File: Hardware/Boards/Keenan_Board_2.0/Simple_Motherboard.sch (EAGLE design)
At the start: 100 parts, among them U1 WIZ811MJ, U1_MUX 74HC4052D,653, U2_MUX 74HC4052D,653, U3_MUX 74HC4052D,653, U4_MUX 74HC4052D,653, U5_MUX 74HC4052D,653, U7_MUX 74HC4052D,653

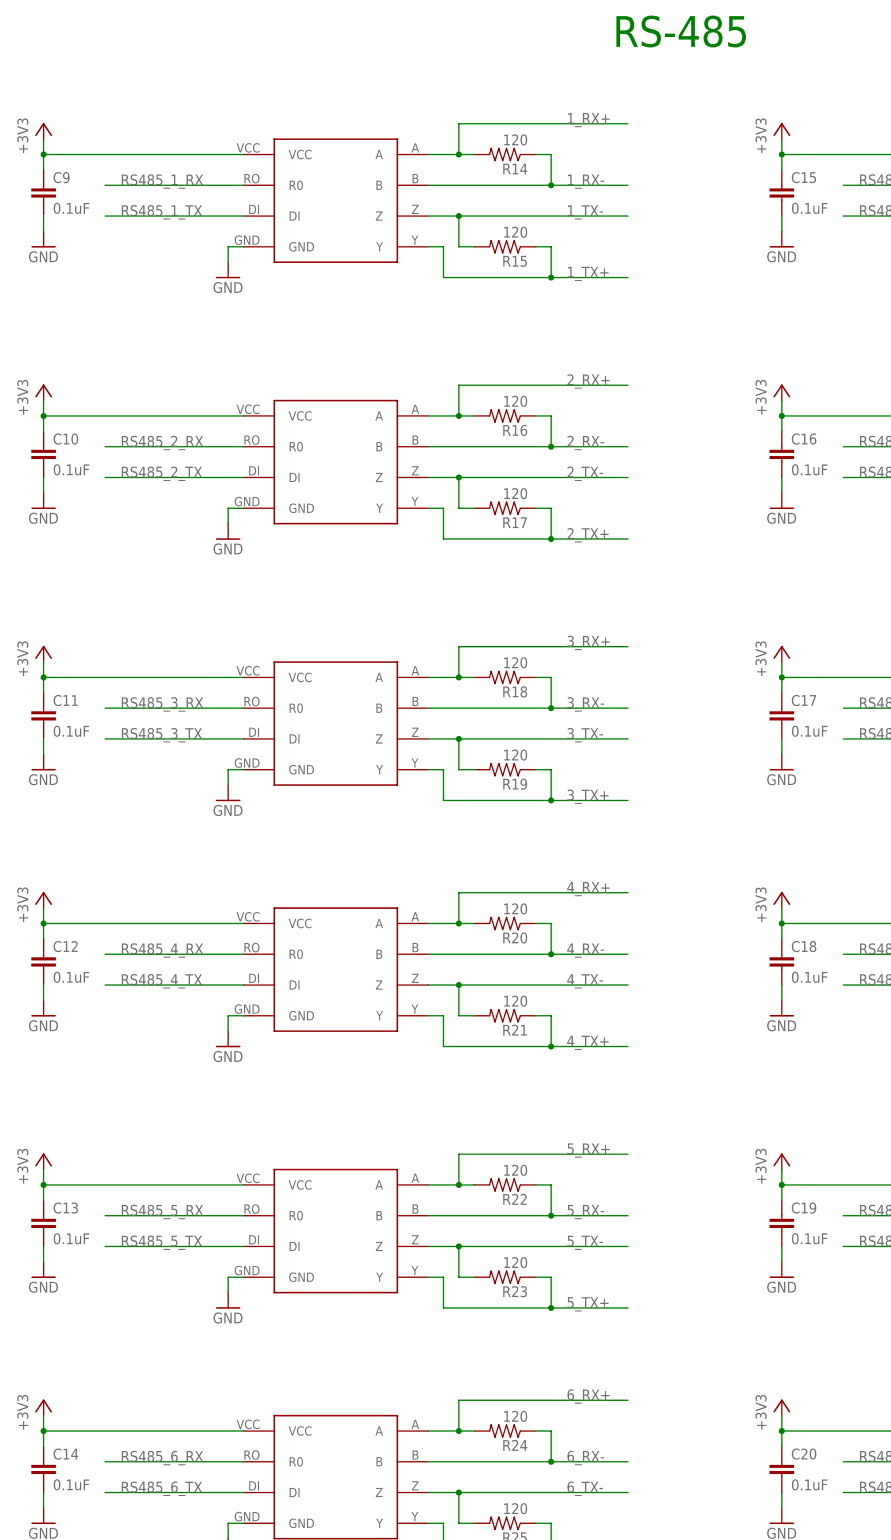
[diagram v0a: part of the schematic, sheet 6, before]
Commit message: Changed muxes back to 5V power.
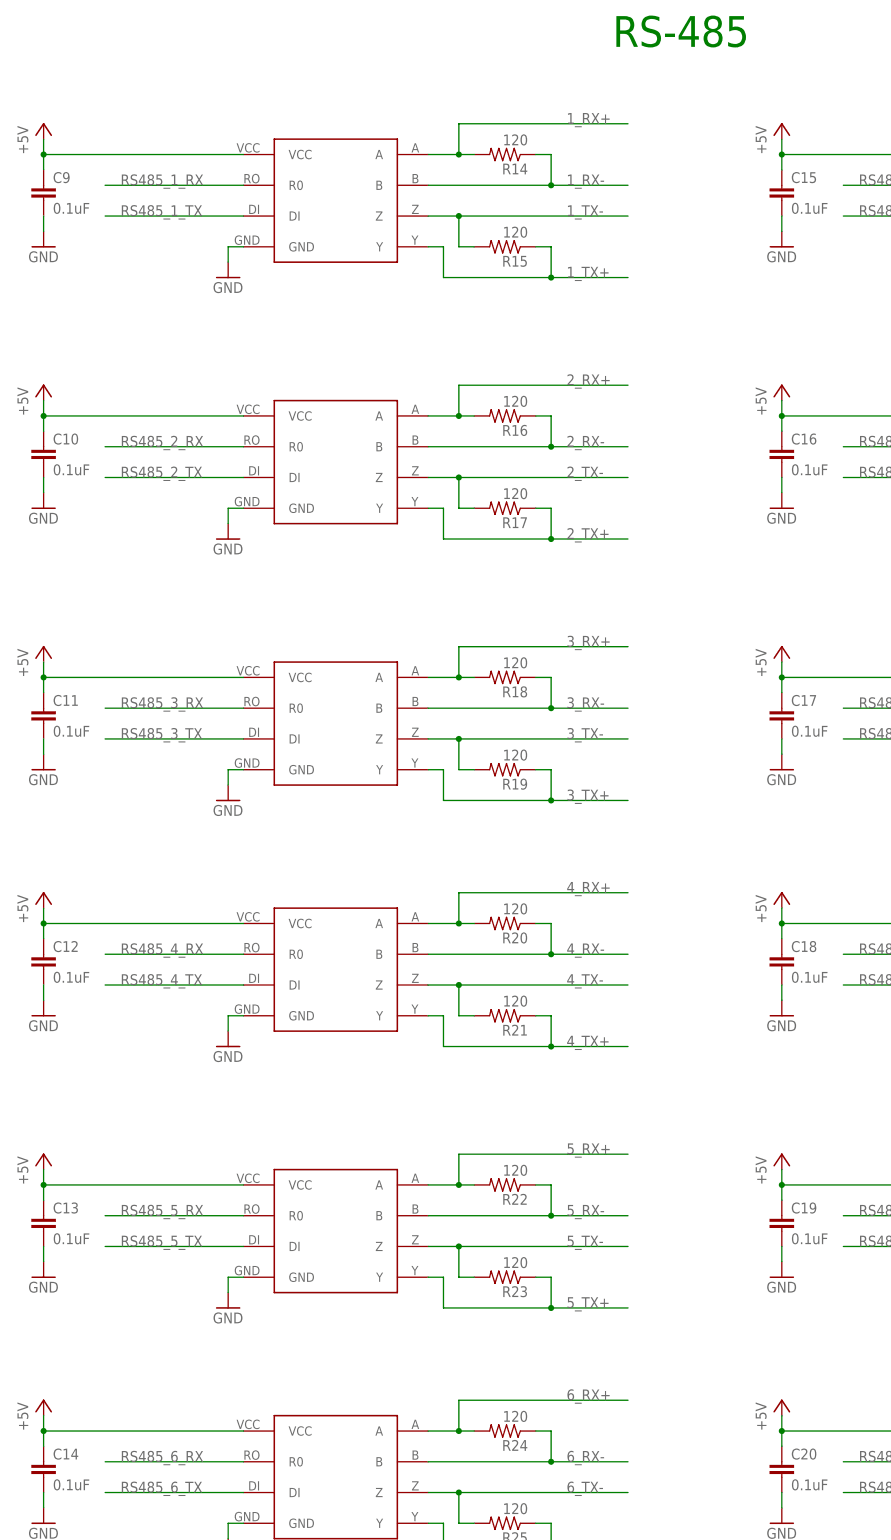
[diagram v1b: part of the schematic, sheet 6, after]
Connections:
- net +3V3: no longer C10.1, C11.1, C12.1, C13.1, C14.1, C15.1, C16.1, C17.1, C18.1, C19.1, C20.1, C3.1, C4.1, C5.1, C6.1, C7.1, C8.1, C9.1, RS-485-1.VCC, RS-485-2.VCC, RS-485-3.VCC, RS-485-4.VCC, RS-485-5.VCC, RS-485-6.VCC, RS_TRANS_1.VCC, RS_TRANS_10.VCC, RS_TRANS_11.VCC, RS_TRANS_12.VCC, RS_TRANS_2.VCC, RS_TRANS_3.VCC, RS_TRANS_4.VCC, RS_TRANS_5.VCC, RS_TRANS_6.VCC, RS_TRANS_7.VCC, RS_TRANS_8.VCC, RS_TRANS_9.VCC
- net +5V: now also C10.1, C11.1, C12.1, C13.1, C14.1, C15.1, C16.1, C17.1, C18.1, C19.1, C20.1, C3.1, C4.1, C5.1, C6.1, C7.1, C8.1, C9.1, RS-485-1.VCC, RS-485-2.VCC, RS-485-3.VCC, RS-485-4.VCC, RS-485-5.VCC, RS-485-6.VCC, RS_TRANS_1.VCC, RS_TRANS_10.VCC, RS_TRANS_11.VCC, RS_TRANS_12.VCC, RS_TRANS_2.VCC, RS_TRANS_3.VCC, RS_TRANS_4.VCC, RS_TRANS_5.VCC, RS_TRANS_6.VCC, RS_TRANS_7.VCC, RS_TRANS_8.VCC, RS_TRANS_9.VCC

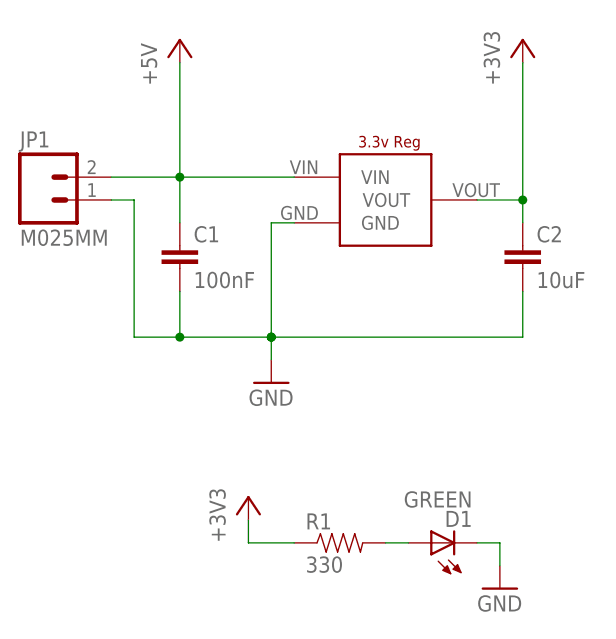
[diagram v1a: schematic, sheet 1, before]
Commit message: Routing power work
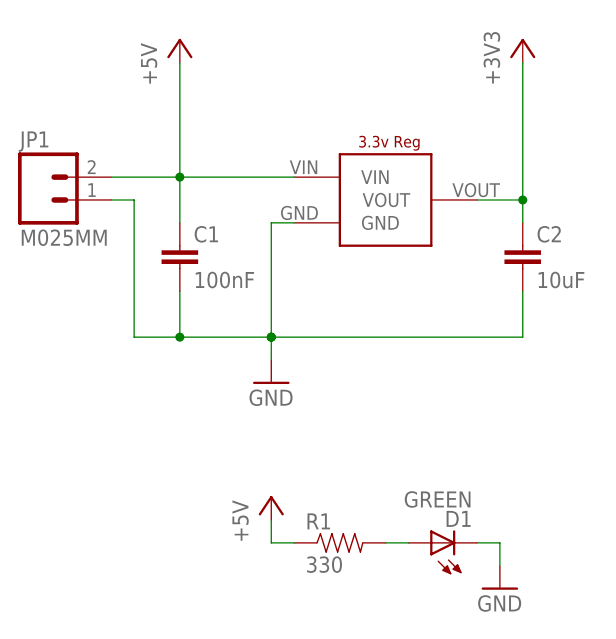
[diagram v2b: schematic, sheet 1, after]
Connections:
- net +3V3: no longer R1.1
- net +5V: now also R1.1, U7_MUX.VCC
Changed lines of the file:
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@@
 <part name="D1" library="SparkFun-LED" deviceset="LED-GREEN" device="LARGE" value="GREEN"/>
 <part name="GND94" library="supply1" deviceset="GND" device=""/>
-<part name="+3V53" library="supply1" deviceset="+3V3" device=""/>
 <part name="R1" library="SparkFun-Passives" deviceset="RESISTOR" device="1206" value="330"/>
 <part name="P+5" library="supply1" deviceset="+5V" device=""/>
@@
 <part name="P+25" library="supply1" deviceset="+5V" device=""/>
 <part name="P+26" library="supply1" deviceset="+5V" device=""/>
+<part name="P+27" library="supply1" deviceset="+5V" device=""/>
 </parts>
 <sheets>
@@
 <instance part="D1" gate="G$1" x="7.62" y="-17.78" rot="R90"/>
 <instance part="GND94" gate="1" x="15.24" y="-22.86"/>
-<instance part="+3V53" gate="G$1" x="-12.7" y="-12.7"/>
 <instance part="R1" gate="G$1" x="-2.54" y="-17.78"/>
 <instance part="P+5" gate="1" x="-20.32" y="38.1"/>
+<instance part="P+27" gate="1" x="-10.16" y="-12.7"/>
 </instances>
 <busses>
@@
 <nets>
 <net name="+3V3" class="0">
-<segment>
-<pinref part="+3V53" gate="G$1" pin="+3V3"/>
-<wire x1="-12.7" y1="-15.24" x2="-12.7" y2="-17.78" width="0.1524" layer="91"/>
-<pinref part="R1" gate="G$1" pin="1"/>
-<wire x1="-12.7" y1="-17.78" x2="-7.62" y2="-17.78" width="0.1524" layer="91"/>
-</segment>
 <segment>
 <pinref part="U$1" gate="G$1" pin="VOUT"/>
@@
 <pinref part="P+5" gate="1" pin="+5V"/>
 <wire x1="-20.32" y1="22.86" x2="-20.32" y2="35.56" width="0.1524" layer="91"/>
+</segment>
+<segment>
+<pinref part="P+27" gate="1" pin="+5V"/>
+<wire x1="-10.16" y1="-15.24" x2="-10.16" y2="-17.78" width="0.1524" layer="91"/>
+<pinref part="R1" gate="G$1" pin="1"/>
+<wire x1="-10.16" y1="-17.78" x2="-7.62" y2="-17.78" width="0.1524" layer="91"/>
 </segment>
 </net>
@@
 </segment>
 <segment>
+<pinref part="C26" gate="G$1" pin="1"/>
+<pinref part="P+7" gate="1" pin="+5V"/>
+<wire x1="66.04" y1="-17.78" x2="66.04" y2="-15.24" width="0.1524" layer="91"/>
+<pinref part="U7_MUX" gate="A" pin="VCC"/>
+<wire x1="66.04" y1="-15.24" x2="66.04" y2="-12.7" width="0.1524" layer="91"/>
 <wire x1="99.06" y1="-15.24" x2="66.04" y2="-15.24" width="0.1524" layer="91"/>
-<pinref part="C26" gate="G$1" pin="1"/>
-<wire x1="66.04" y1="-15.24" x2="66.04" y2="-17.78" width="0.1524" layer="91"/>
-<pinref part="P+7" gate="1" pin="+5V"/>
-<wire x1="66.04" y1="-15.24" x2="66.04" y2="-12.7" width="0.1524" layer="91"/>
 <junction x="66.04" y="-15.24"/>
 </segment>

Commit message: More routing
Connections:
- net +5V: now also U2_MUX.VCC, U3_MUX.VCC, U4_MUX.VCC, U5_MUX.VCC
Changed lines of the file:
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@@
 </segment>
 <segment>
+<pinref part="C22" gate="G$1" pin="1"/>
+<pinref part="P+2" gate="1" pin="+5V"/>
+<wire x1="-50.8" y1="40.64" x2="-50.8" y2="43.18" width="0.1524" layer="91"/>
+<pinref part="U2_MUX" gate="A" pin="VCC"/>
+<wire x1="-50.8" y1="43.18" x2="-50.8" y2="45.72" width="0.1524" layer="91"/>
 <wire x1="-17.78" y1="43.18" x2="-50.8" y2="43.18" width="0.1524" layer="91"/>
-<pinref part="C22" gate="G$1" pin="1"/>
-<wire x1="-50.8" y1="43.18" x2="-50.8" y2="40.64" width="0.1524" layer="91"/>
-<pinref part="P+2" gate="1" pin="+5V"/>
-<wire x1="-50.8" y1="43.18" x2="-50.8" y2="45.72" width="0.1524" layer="91"/>
 <junction x="-50.8" y="43.18"/>
 </segment>
 <segment>
+<pinref part="C23" gate="G$1" pin="1"/>
+<pinref part="P+3" gate="1" pin="+5V"/>
+<wire x1="66.04" y1="40.64" x2="66.04" y2="43.18" width="0.1524" layer="91"/>
+<pinref part="U3_MUX" gate="A" pin="VCC"/>
+<wire x1="66.04" y1="43.18" x2="66.04" y2="45.72" width="0.1524" layer="91"/>
 <wire x1="99.06" y1="43.18" x2="66.04" y2="43.18" width="0.1524" layer="91"/>
-<pinref part="C23" gate="G$1" pin="1"/>
-<wire x1="66.04" y1="43.18" x2="66.04" y2="40.64" width="0.1524" layer="91"/>
-<pinref part="P+3" gate="1" pin="+5V"/>
-<wire x1="66.04" y1="43.18" x2="66.04" y2="45.72" width="0.1524" layer="91"/>
 <junction x="66.04" y="43.18"/>
 </segment>
 <segment>
+<pinref part="C24" gate="G$1" pin="1"/>
+<pinref part="P+4" gate="1" pin="+5V"/>
+<wire x1="-165.1" y1="-17.78" x2="-165.1" y2="-15.24" width="0.1524" layer="91"/>
+<pinref part="U4_MUX" gate="A" pin="VCC"/>
+<wire x1="-165.1" y1="-15.24" x2="-165.1" y2="-12.7" width="0.1524" layer="91"/>
 <wire x1="-132.08" y1="-15.24" x2="-165.1" y2="-15.24" width="0.1524" layer="91"/>
-<pinref part="C24" gate="G$1" pin="1"/>
-<wire x1="-165.1" y1="-15.24" x2="-165.1" y2="-17.78" width="0.1524" layer="91"/>
-<pinref part="P+4" gate="1" pin="+5V"/>
-<wire x1="-165.1" y1="-15.24" x2="-165.1" y2="-12.7" width="0.1524" layer="91"/>
 <junction x="-165.1" y="-15.24"/>
 </segment>
 <segment>
+<pinref part="C25" gate="G$1" pin="1"/>
+<pinref part="P+6" gate="1" pin="+5V"/>
+<wire x1="-50.8" y1="-17.78" x2="-50.8" y2="-15.24" width="0.1524" layer="91"/>
+<pinref part="U5_MUX" gate="A" pin="VCC"/>
+<wire x1="-50.8" y1="-15.24" x2="-50.8" y2="-12.7" width="0.1524" layer="91"/>
 <wire x1="-17.78" y1="-15.24" x2="-50.8" y2="-15.24" width="0.1524" layer="91"/>
-<pinref part="C25" gate="G$1" pin="1"/>
-<wire x1="-50.8" y1="-15.24" x2="-50.8" y2="-17.78" width="0.1524" layer="91"/>
-<pinref part="P+6" gate="1" pin="+5V"/>
-<wire x1="-50.8" y1="-15.24" x2="-50.8" y2="-12.7" width="0.1524" layer="91"/>
 <junction x="-50.8" y="-15.24"/>
 </segment>

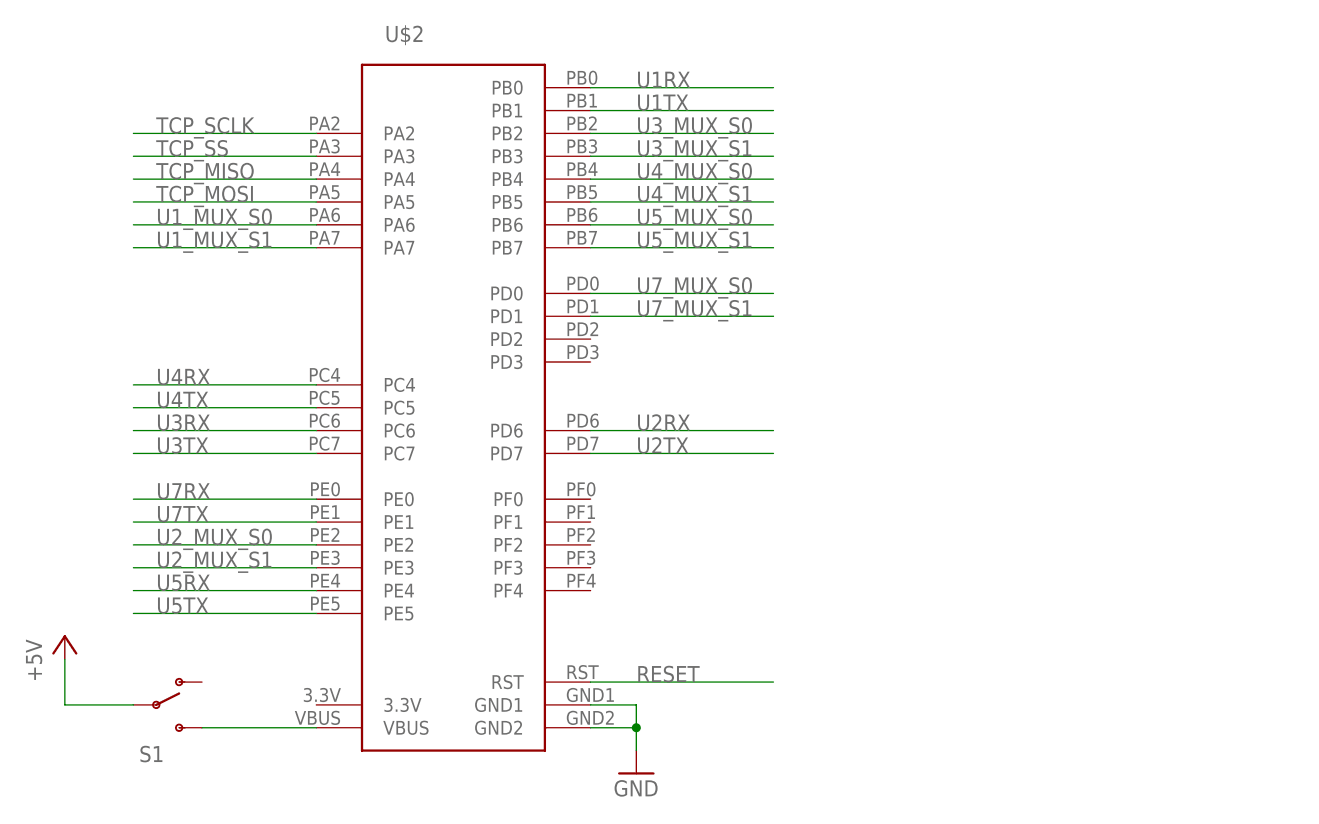
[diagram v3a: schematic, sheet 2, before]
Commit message: Added LCD Headers
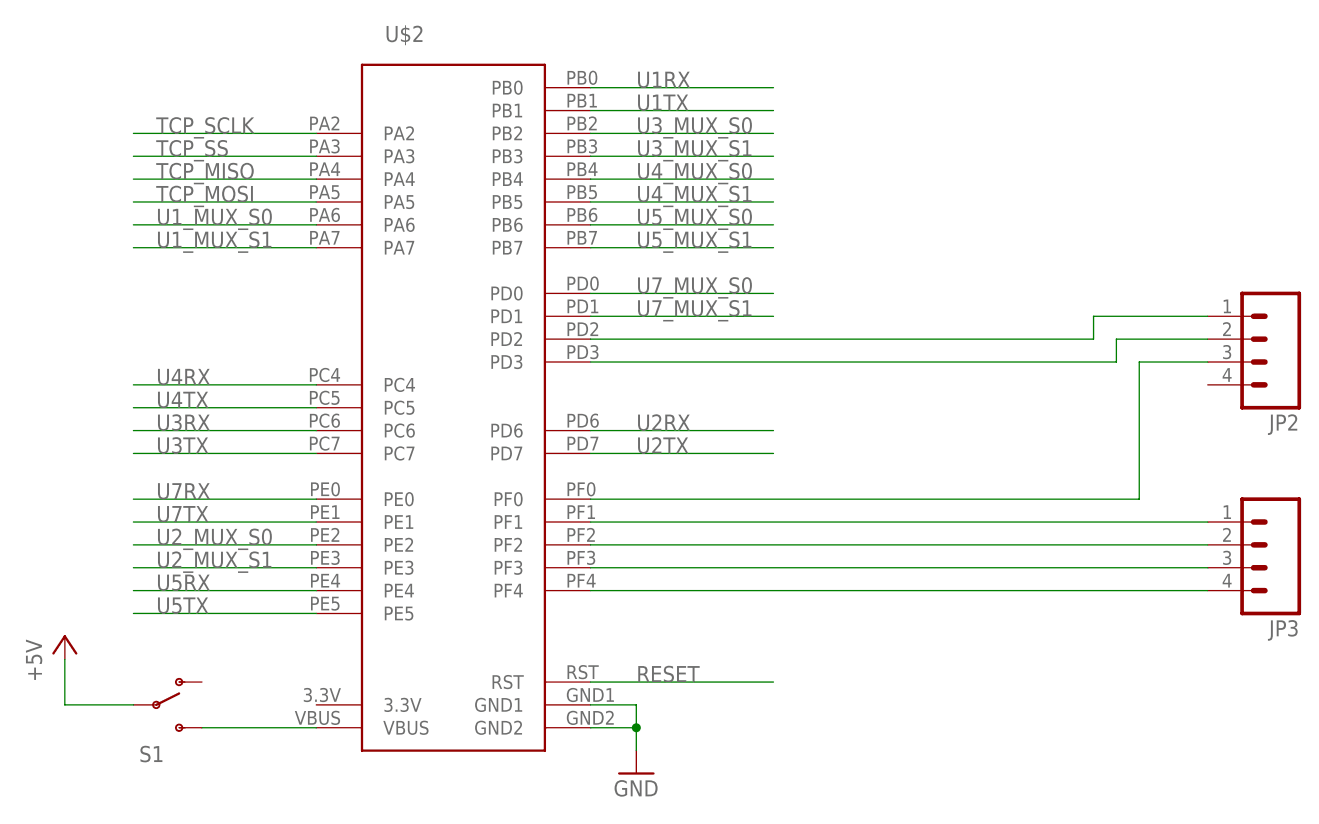
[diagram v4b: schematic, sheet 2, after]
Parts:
- added JP2, JP3: (no value), SparkFun-Connectors:M04POLAR
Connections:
- new net N$23: JP2.2, U$2.PD3
- new net N$24: JP2.3, U$2.PF0
- new net N$25: JP3.1, U$2.PF1
- new net N$26: JP3.2, U$2.PF2
- new net N$27: JP3.3, U$2.PF3
- new net N$30: JP3.4, U$2.PF4
- new net N$7: JP2.1, U$2.PD2
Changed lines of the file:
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@@
 <part name="P+26" library="supply1" deviceset="+5V" device=""/>
 <part name="P+27" library="supply1" deviceset="+5V" device=""/>
+<part name="JP2" library="SparkFun-Connectors" deviceset="M04" device="POLAR"/>
+<part name="JP3" library="SparkFun-Connectors" deviceset="M04" device="POLAR"/>
 </parts>
 <sheets>
@@
 <instance part="S1" gate="1" x="-33.02" y="-35.56"/>
 <instance part="U$2" gate="G$1" x="0" y="0"/>
+<instance part="JP2" gate="G$1" x="88.9" y="5.08" rot="R180"/>
+<instance part="JP3" gate="G$1" x="88.9" y="-17.78" rot="R180"/>
 </instances>
 <busses>
@@
 </segment>
 </net>
+<net name="N$7" class="0">
+<segment>
+<pinref part="U$2" gate="G$1" pin="PD2"/>
+<wire x1="15.24" y1="5.08" x2="71.12" y2="5.08" width="0.1524" layer="91"/>
+<wire x1="71.12" y1="5.08" x2="71.12" y2="7.62" width="0.1524" layer="91"/>
+<pinref part="JP2" gate="G$1" pin="1"/>
+<wire x1="71.12" y1="7.62" x2="83.82" y2="7.62" width="0.1524" layer="91"/>
+</segment>
+</net>
+<net name="N$23" class="0">
+<segment>
+<pinref part="U$2" gate="G$1" pin="PD3"/>
+<wire x1="15.24" y1="2.54" x2="73.66" y2="2.54" width="0.1524" layer="91"/>
+<wire x1="73.66" y1="2.54" x2="73.66" y2="5.08" width="0.1524" layer="91"/>
+<pinref part="JP2" gate="G$1" pin="2"/>
+<wire x1="73.66" y1="5.08" x2="83.82" y2="5.08" width="0.1524" layer="91"/>
+</segment>
+</net>
+<net name="N$24" class="0">
+<segment>
+<pinref part="U$2" gate="G$1" pin="PF0"/>
+<wire x1="15.24" y1="-12.7" x2="76.2" y2="-12.7" width="0.1524" layer="91"/>
+<wire x1="76.2" y1="-12.7" x2="76.2" y2="2.54" width="0.1524" layer="91"/>
+<pinref part="JP2" gate="G$1" pin="3"/>
+<wire x1="76.2" y1="2.54" x2="83.82" y2="2.54" width="0.1524" layer="91"/>
+</segment>
+</net>
+<net name="N$25" class="0">
+<segment>
+<pinref part="U$2" gate="G$1" pin="PF1"/>
+<pinref part="JP3" gate="G$1" pin="1"/>
+<wire x1="15.24" y1="-15.24" x2="83.82" y2="-15.24" width="0.1524" layer="91"/>
+</segment>
+</net>
+<net name="N$26" class="0">
+<segment>
+<pinref part="JP3" gate="G$1" pin="2"/>
+<pinref part="U$2" gate="G$1" pin="PF2"/>
+<wire x1="83.82" y1="-17.78" x2="15.24" y2="-17.78" width="0.1524" layer="91"/>
+</segment>
+</net>
+<net name="N$27" class="0">
+<segment>
+<pinref part="JP3" gate="G$1" pin="3"/>
+<pinref part="U$2" gate="G$1" pin="PF3"/>
+<wire x1="83.82" y1="-20.32" x2="15.24" y2="-20.32" width="0.1524" layer="91"/>
+</segment>
+</net>
+<net name="N$30" class="0">
+<segment>
+<pinref part="JP3" gate="G$1" pin="4"/>
+<pinref part="U$2" gate="G$1" pin="PF4"/>
+<wire x1="83.82" y1="-22.86" x2="15.24" y2="-22.86" width="0.1524" layer="91"/>
+</segment>
+</net>
